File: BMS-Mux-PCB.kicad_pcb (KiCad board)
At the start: 2 copper layers, 50 parts, among them J1 Conn_02x08_Counter_Clockwise, J2 Conn_02x08_Counter_Clockwise, J3 Conn_02x09_Counter_Clockwise, J4 Conn_01x17, J5 Conn_01x02, J6 Conn_02x10_Counter_Clockwise, Q1 BSS123, Q2 BSS123, U1 74CBTLV3257, U2 74CBTLV3257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

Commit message: progress
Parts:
- added H1: MountingHole_Pad, BMS-Mux-footprints:Mounting_Hole, F.Cu at (158.0, 55.5)
- added H2: MountingHole_Pad, BMS-Mux-footprints:Mounting_Hole, F.Cu at (70.5, 55.5)
- added H3: MountingHole_Pad, BMS-Mux-footprints:Mounting_Hole, F.Cu at (158.0, 131.5)
- added H4: MountingHole_Pad, BMS-Mux-footprints:Mounting_Hole, F.Cu at (70.5, 131.5)
- F1, F10, F11, F12, F13, F14, F15, F16, F2, F3, F4, F5, F6, F7, F8, F9: footprint Fuse:Fuse_2512_6332Metric_Pad1.52x3.35mm_HandSolder -> Fuse:Fuse_1206_3216Metric_Pad1.42x1.75mm_HandSolder
- J4: value Conn_01x17 -> Conn_01x18; footprint Connector_TE-Connectivity:TE_1-826576-7_1x17_P3.96mm_Vertical -> Connector_Wago:Wago_734-148_1x18_P3.50mm_Vertical
- J6: footprint Connector_Molex:Molex_Micro-Fit_3.0_43045-2000_2x10_P3.00mm_Horizontal -> Connector_PinHeader_2.54mm:PinHeader_2x10_P2.54mm_Vertical; moved to B.Cu
- moved J3 101.5 mm to (109.6, 124.5), turned to 90 degrees
- moved F13 94.9 mm to (69.0, 111.0), turned to 180 degrees
- moved F14 93.6 mm to (69.0, 114.5), turned to 180 degrees
- moved F15 92.4 mm to (69.0, 118.0), turned to 180 degrees
- moved F16 91.1 mm to (69.0, 121.5), turned to 180 degrees
- moved J5 88.6 mm to (104.5, 63.0), turned to 90 degrees
- moved U3 76.4 mm to (114.0, 54.9), turned to -90 degrees
- moved F7 72.1 mm to (69.0, 90.0), turned to 180 degrees
- moved U1 71.2 mm to (159.0, 67.5), turned to 180 degrees
- moved F8 70.8 mm to (69.0, 93.5), turned to 180 degrees
- moved F9 69.5 mm to (69.0, 97.0), turned to 180 degrees
- moved F10 68.2 mm to (69.0, 100.5), turned to 180 degrees
- moved F11 66.9 mm to (69.0, 104.0), turned to 180 degrees
- moved F12 65.7 mm to (69.0, 107.5), turned to 180 degrees
- moved C4 59.7 mm to (118.2, 55.0), turned to 90 degrees
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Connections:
- U1 pad 15: +3V3 -> GND
- U2 pad 15: +3V3 -> GND
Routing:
- net /BATT_16: track 0.00 -> 4.99 mm
- net /BATT_15: track 0.00 -> 4.69 mm
- net /BATT_9: track 0.00 -> 4.60 mm
- net /BATT_8: track 0.00 -> 4.60 mm
- net /BATT_7: track 0.00 -> 4.60 mm
- net /BATT_6: track 0.00 -> 4.60 mm
- net /BATT_5: track 0.00 -> 4.60 mm
- net /BATT_4: track 0.00 -> 4.60 mm
- net /BATT_2: track 0.00 -> 4.60 mm
- net /BATT_14: track 0.00 -> 4.60 mm
- net /BATT_13: track 0.00 -> 4.60 mm
- net /BATT_11: track 0.00 -> 4.60 mm
- net /BATT_10: track 0.00 -> 4.60 mm
- net /BATT_3: track 0.00 -> 4.59 mm
- net /BATT_12: track 0.00 -> 4.59 mm
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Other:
- board outline added: 113.5 x 88 mm

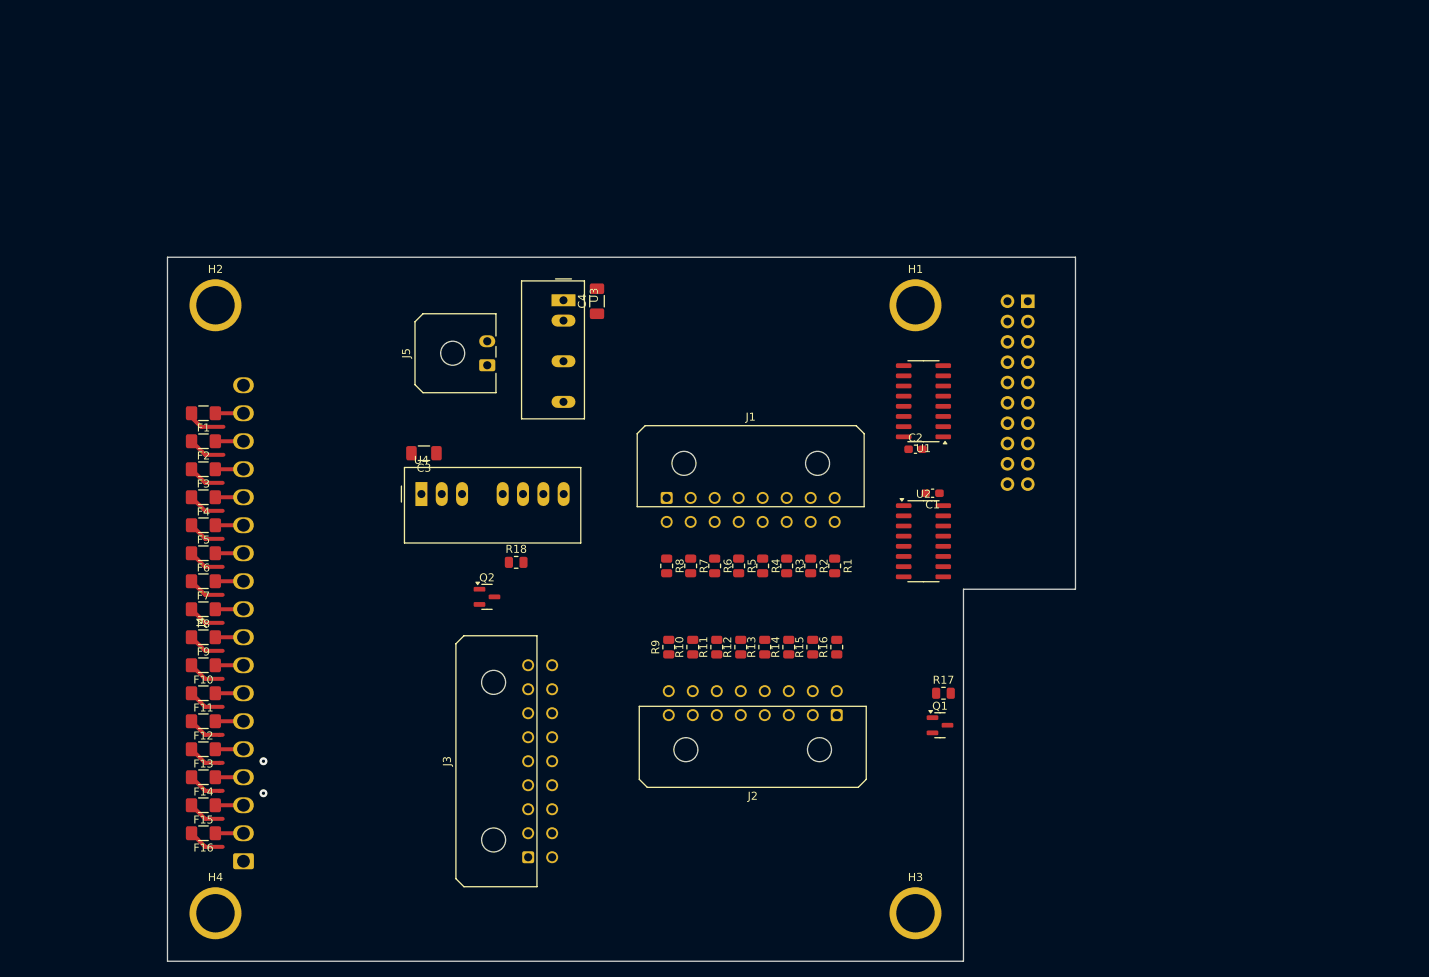
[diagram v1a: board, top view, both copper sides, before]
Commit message: updated footprints and started layout
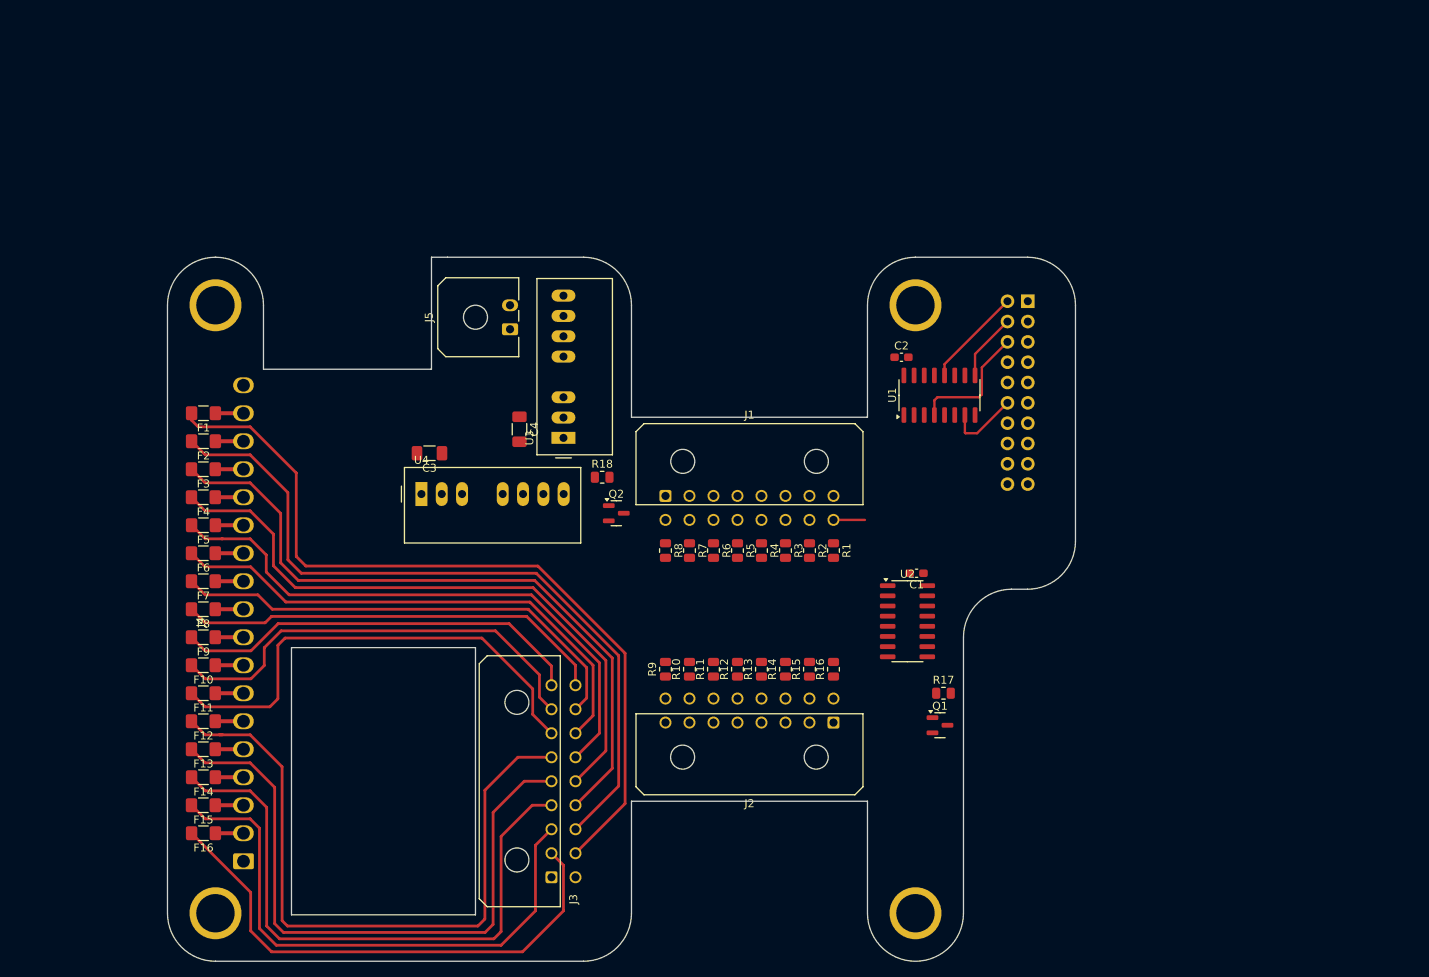
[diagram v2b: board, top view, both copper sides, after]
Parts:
- J1, J2: footprint Connector_Molex:Molex_Micro-Fit_3.0_43045-1600_2x08_P3.00mm_Horizontal -> BMS-Mux-footprints:Molex_Micro-Fit_3.0_43045-1600_2x08_P3.00mm_Horizontal
- J3: value Conn_02x09_Counter_Clockwise -> Conn_02x09_Top_Bottom; footprint Connector_Molex:Molex_Micro-Fit_3.0_43045-1800_2x09_P3.00mm_Horizontal -> BMS-Mux-footprints:Molex_Micro-Fit_3.0_43045-1800_2x09_P3.00mm_Horizontal
- J5: footprint Connector_Molex:Molex_Micro-Fit_3.0_43650-0200_1x02_P3.00mm_Horizontal -> BMS-Mux-footprints:Molex_Micro-Fit_3.0_43650-0200_1x02_P3.00mm_Horizontal
- J6: value Conn_02x10_Counter_Clockwise -> Conn_02x10_Odd_Even
- U3: value TMR_1-4812 -> TEC2-4812WI; footprint Converter_DCDC:Converter_DCDC_TRACO_TMR-1-xxxx_Single_THT -> Converter_DCDC:Converter_DCDC_TRACO_TMR-xxxx_THT
- moved Q2 19.2 mm to (120.6, 81.5)
- moved C4 18.7 mm to (108.5, 71.0), turned to -90 degrees
- moved U3 17.2 mm to (114.0, 72.1), turned to 90 degrees
- moved R18 15.1 mm to (118.8, 77.0)
- moved C2 11.6 mm to (156.2, 62.0)
- moved C1 10.2 mm to (158.1, 89.0)
- moved U2 10.2 mm to (157.0, 95.0)
- moved J5 5.33 mm to (107.3, 58.5)
- moved J3 3.84 mm to (112.5, 127.0)
- moved R10 2.80 mm to (129.8, 101.0)
- moved R11 2.80 mm to (132.8, 101.0)
- moved R12 2.80 mm to (135.8, 101.0)
- moved R13 2.80 mm to (138.8, 101.0)
- moved R14 2.80 mm to (141.8, 101.0)
- moved R15 2.80 mm to (144.8, 101.0)
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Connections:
- J3 pad 10: /BATT_9 -> unconnected-(J3-Pin_10-Pad10)
- J3 pad 11: /BATT_10 -> /BATT_16
- J3 pad 12: /BATT_11 -> /BATT_15
- J3 pad 13: /BATT_12 -> /BATT_14
- J3 pad 15: /BATT_14 -> /BATT_12
- J3 pad 16: /BATT_15 -> /BATT_11
- J3 pad 17: /BATT_16 -> /BATT_10
- J3 pad 18: unconnected-(J3-Pin_18-Pad18) -> /BATT_9
- J6 pad 1: /GPIO1_ADC -> GND
- J6 pad 10: /GPIO10_ADC -> /GPIO6_EN
- J6 pad 12: GND -> /GPIO6_ADC
- J6 pad 14: GND -> /GPIO7_ADC
- J6 pad 16: GND -> /GPIO8_ADC
- J6 pad 18: GND -> /GPIO9_ADC
- J6 pad 2: /GPIO2_ADC -> /GPIO1_ADC
- J6 pad 20: GND -> /GPIO10_ADC
- J6 pad 3: /GPIO3_ADC -> GND
- J6 pad 4: /GPIO5_SW -> /GPIO2_ADC
- J6 pad 5: /GPIO6_EN -> GND
- J6 pad 6: /GPIO6_ADC -> /GPIO3_ADC
- J6 pad 7: /GPIO7_ADC -> GND
- J6 pad 8: /GPIO8_ADC -> /GPIO5_SW
- J6 pad 9: /GPIO9_ADC -> GND
- U1 pad 10: /SENS_6 -> /SENS_4
- U1 pad 11: /SENS_5 -> /SENS_3
- U1 pad 12: /GPIO6_ADC -> /GPIO1_ADC
- U1 pad 13: /SENS_8 -> /SENS_2
- U1 pad 14: /SENS_7 -> /SENS_1
- U1 pad 2: /SENS_1 -> /SENS_5
- U1 pad 3: /SENS_2 -> /SENS_6
- U1 pad 4: /GPIO1_ADC -> /GPIO3_ADC
- U1 pad 5: /SENS_3 -> /SENS_7
- U1 pad 6: /SENS_4 -> /SENS_8
- U1 pad 7: /GPIO2_ADC -> /GPIO6_ADC
- U1 pad 9: /GPIO3_ADC -> /GPIO2_ADC
- U3 pad 6: Net-(J5-Pin_2) -> Net-(J5-Pin_1)
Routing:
- net /BATT_16: track 4.99 -> 100.8 mm
- net /BATT_15: track 4.69 -> 93.3 mm
- net /BATT_14: track 4.60 -> 86.3 mm
- net /BATT_5: track 4.60 -> 85.4 mm
- net /BATT_4: track 4.60 -> 80.5 mm
- net /BATT_13: track 4.60 -> 79.2 mm
- net /BATT_3: track 4.59 -> 75.9 mm
- net /BATT_12: track 4.59 -> 72.5 mm
- net /BATT_2: track 4.60 -> 70.4 mm
- net /BATT_11: track 4.60 -> 65.4 mm
- net /BATT_1: track 4.59 -> 65.4 mm
- net /BATT_6: track 4.60 -> 60.0 mm
- net /BATT_10: track 4.60 -> 59.7 mm
- net /BATT_7: track 4.60 -> 55.2 mm
- net /BATT_9: track 4.60 -> 54.1 mm
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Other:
- outline, holes or cut-outs redrawn
